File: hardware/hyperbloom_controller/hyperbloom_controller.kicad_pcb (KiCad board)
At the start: 2 copper layers, 61 x 54 mm, 13 parts, among them J1 SMA connector ?, J3 Left side header, J4 Right side header

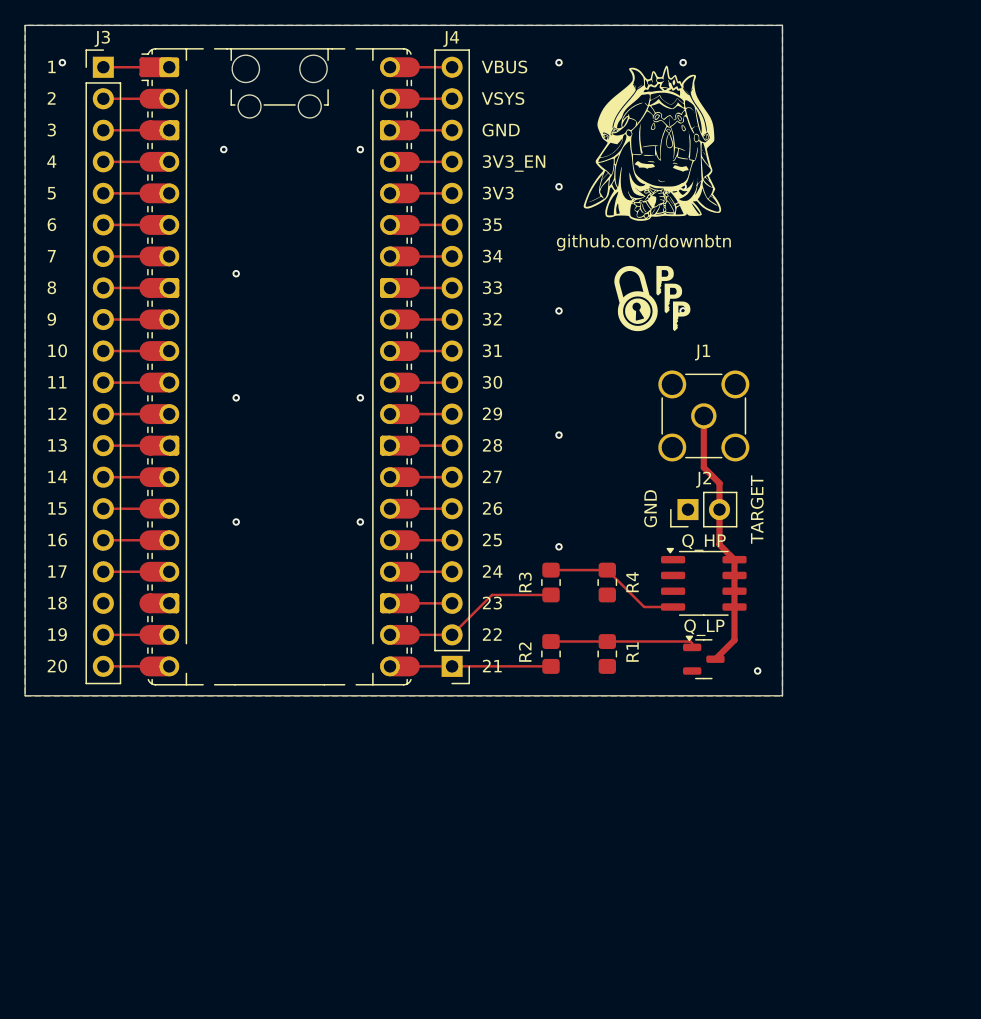
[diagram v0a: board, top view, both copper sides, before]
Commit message: Controller PCB v0.1
I designed this a while ago but forgot to commit

Mainly just cleaned up the routing
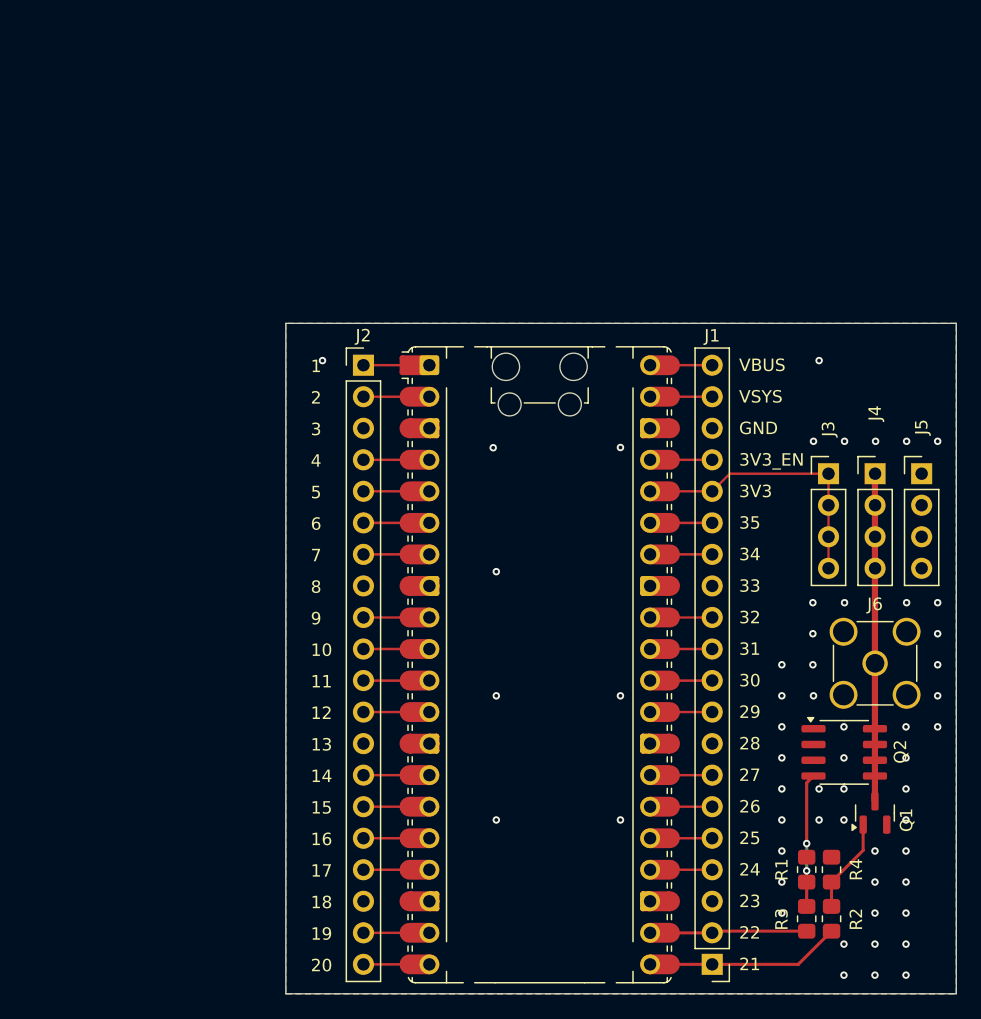
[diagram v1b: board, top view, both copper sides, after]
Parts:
- removed GND: glitch pin, Connector_PinHeader_2.54mm:PinHeader_1x02_P2.54mm_Vertical
- removed the J1 at (154.7, 81.5)
- added J3: Extra 3V3, Connector_PinHeader_2.54mm:PinHeader_1x04_P2.54mm_Vertical, F.Cu at (164.7, 86.1)
- added J4: Glitch pin, Connector_PinHeader_2.54mm:PinHeader_1x04_P2.54mm_Vertical, F.Cu at (168.5, 86.1)
- added J5: Extra GND, Connector_PinHeader_2.54mm:PinHeader_1x04_P2.54mm_Vertical, F.Cu at (172.2, 86.1)
- added J6: SMA glitch connector, Connector_Coaxial:SMA_Amphenol_901-144_Vertical, F.Cu at (168.5, 101.4)
- G*** (x2): moved to B.Cu
- J1: renamed from J4; value Right side header -> Pico right header
- J2: renamed from J3; value Left side header -> Pico left header
- moved G*** 56.2 mm to (170.5, 124.5), turned to 180 degrees
- moved G*** 54.3 mm to (166.0, 111.5), turned to 180 degrees
- moved R3 34.0 mm to (162.9, 122.0)
- moved J1 31.9 mm to (155.3, 125.6)
- moved J2 31.9 mm to (127.2, 77.4)
- moved A1 31.9 mm to (141.4, 101.5)
- moved R2 31.1 mm to (164.9, 122.0)
- moved R4 28.2 mm to (162.9, 118.0), turned to 90 degrees
- moved R1 25.1 mm to (164.9, 118.0), turned to 90 degrees
- moved Q1 18.5 mm to (168.4, 113.4), turned to 90 degrees
- moved Q2 17.7 mm to (166.0, 108.6)
- renumbered Q_LP to Q1, Q_HP to Q2
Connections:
- net Net-(A1-3V3) renamed /3V3
- net Net-(A1-3V3_EN) renamed /3V3_EN
- net Net-(A1-ADC_VREF) renamed /ADC_VREF
- net Net-(A1-GPIO0) renamed /GPIO0
- net Net-(A1-GPIO1) renamed /GPIO1
- net Net-(A1-GPIO10) renamed /GPIO10
- net Net-(A1-GPIO11) renamed /GPIO11
- net Net-(A1-GPIO12) renamed /GPIO12
- net Net-(A1-GPIO13) renamed /GPIO13
- net Net-(A1-GPIO14) renamed /GPIO14
- net Net-(A1-GPIO15) renamed /GPIO15
- net Net-(A1-GPIO16) renamed /GPIO16
- net Net-(A1-GPIO17) renamed /GPIO17
- net Net-(A1-GPIO18) renamed /GPIO18
- net Net-(A1-GPIO19) renamed /GPIO19
- net Net-(A1-GPIO2) renamed /GPIO2
- net Net-(A1-GPIO20) renamed /GPIO20
- net Net-(A1-GPIO21) renamed /GPIO21
- net Net-(A1-GPIO22) renamed /GPIO22
- net Net-(A1-GPIO26_ADC0) renamed /GPIO26
- net Net-(A1-GPIO27_ADC1) renamed /GPIO27
- net Net-(A1-GPIO28_ADC2) renamed /GPIO28
- net Net-(A1-GPIO3) renamed /GPIO3
- net Net-(A1-GPIO4) renamed /GPIO4
- net Net-(A1-GPIO5) renamed /GPIO5
- net Net-(A1-GPIO6) renamed /GPIO6
- net Net-(A1-GPIO7) renamed /GPIO7
- net Net-(A1-GPIO8) renamed /GPIO8
- net Net-(A1-GPIO9) renamed /GPIO9
- net Net-(A1-RUN) renamed /RUN
- net Net-(A1-VBUS) renamed /VBUS
- net Net-(A1-VSYS) renamed /VSYS
- net Net-(J1-In) renamed /GLITCH
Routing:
- net GND: track 35.1 -> 0.00 mm, vias 17 -> 56
- net /3V3: track 5.00 -> 22.7 mm
- net /GLITCH: track 21.3 -> 29.0 mm
- net Net-(Q1-G): track 11.8 -> 7.68 mm
- net /GPIO16: track 13.0 -> 15.7 mm
- net /GPIO17: track 14.3 -> 13.2 mm
- net Net-(Q2-G): track 11.1 -> 10.8 mm, vias 0 -> 2
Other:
- board size 61 x 54 mm -> 54 x 54 mm
- board text added: "Hyperbloom v0.1 github.com/downbtn 2025"
- board text removed: "J2"
- board text removed: "TARGET"
- board text removed: "github.com/downbtn"
